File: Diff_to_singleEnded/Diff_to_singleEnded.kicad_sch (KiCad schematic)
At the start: 45 parts, among them IC1 ULN2003LVDR, J1 1725672, J2 1725672, J3 1725672, J4 1725672, J5 1725672, J6 1725672, J7 1725672, K3 EE2-5NU, U1 OPA1692xD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

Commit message: removed Relay and power supples related items from board and add seperate ground plains for signal and power
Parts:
- removed C11: 100n, Capacitor_SMD:C_0805_2012Metric_Pad1.18x1.45mm_HandSolder, symbol Device:C
- removed IC1: ULN2003LVDR, samsys:SOIC127P780X200-16N, symbol SamaSys:ULN2003LVDR
- removed J2, J6, J7: 1725672, 1725672, symbol NewSamsys:1725672
- removed K3: EE2-5NU, EE2-5NU, symbol NewSamsys:EE2-5NU
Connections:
- net right in is gone; now on net Rout: C2.2, R10.2, U3.7
- net right out is gone; now on net Lout: J3.1
- net GND: no longer C13.1, C14.1, C15.1, J3.2, J3.3, J4.2, J4.3, J5.2, J5.3, R5.2, R6.1, R8.1
- net Left Out renamed Rout
- net Left in renamed Lout
- new net GND 2: C13.1, C14.1, C15.1, J3.2, J3.3, J4.2, J4.3, J5.2, J5.3, R5.2, R6.1, R8.1
- no-connect marks 14 -> 0
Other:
- moved on the sheet: C1, C10, C12, C13, C14, C15, C2, C3, C4, C5, C6, C7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

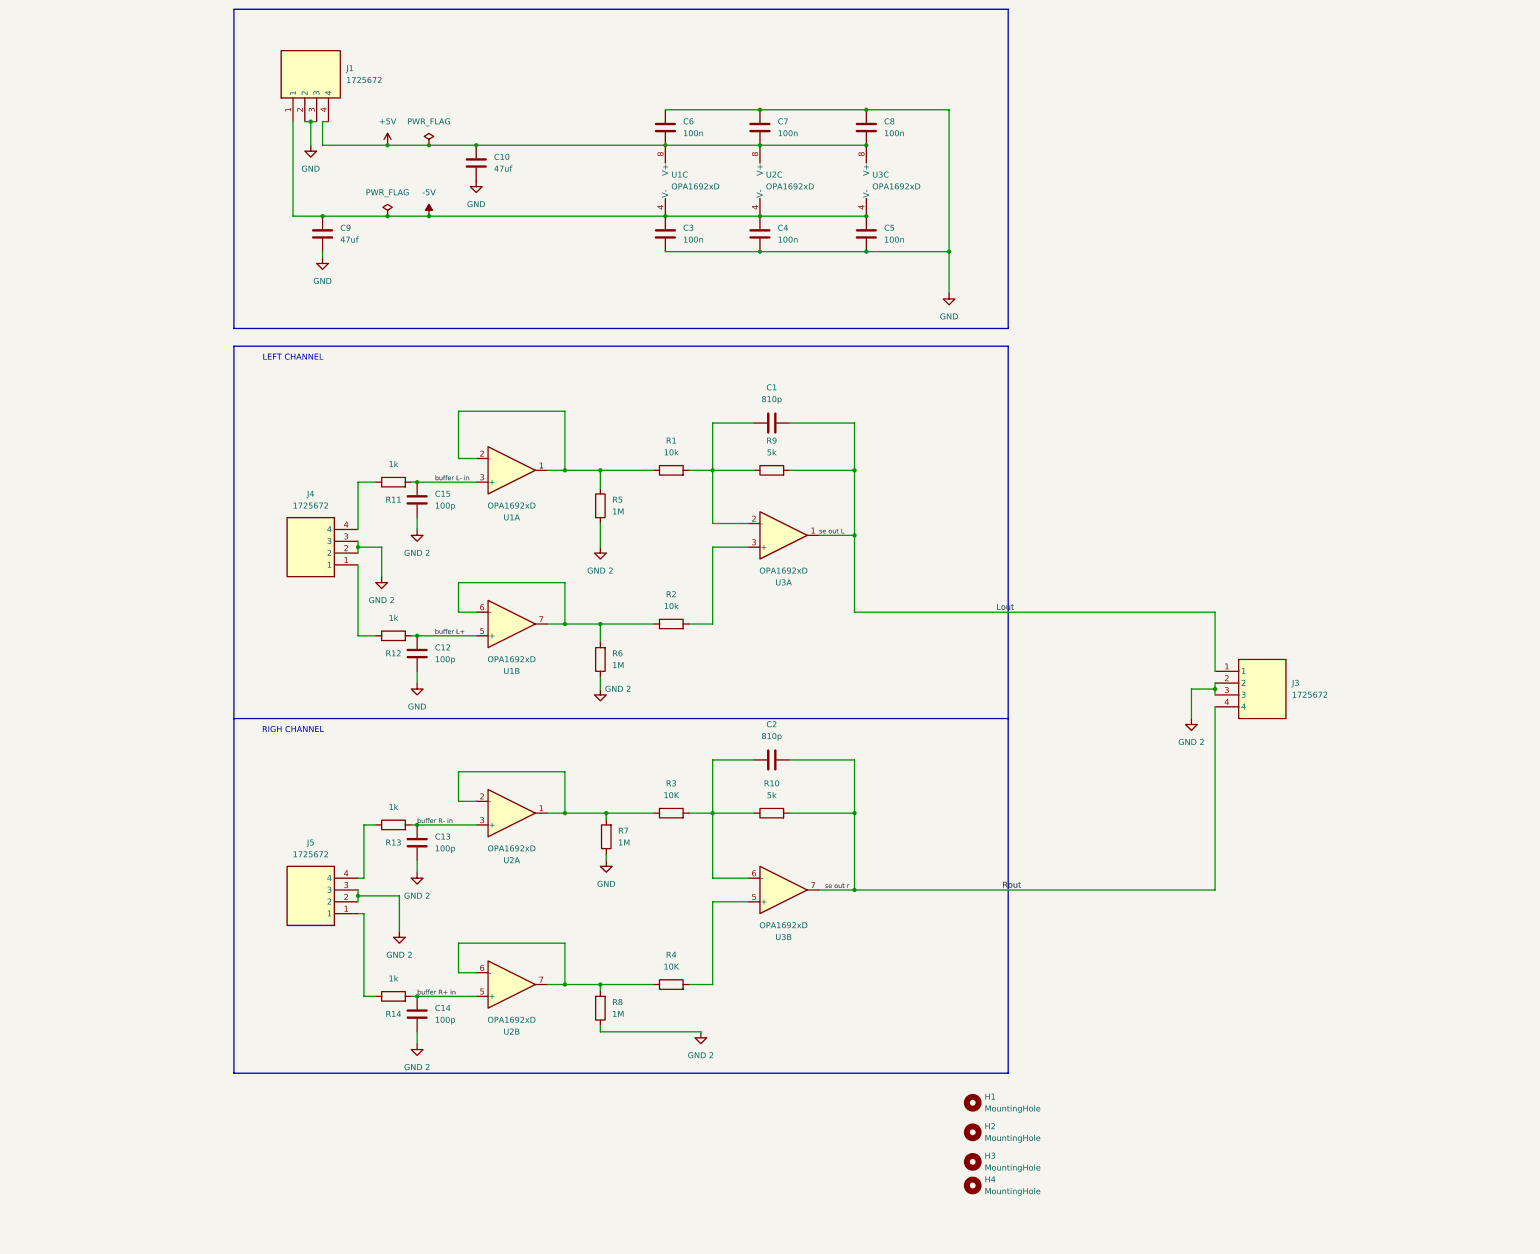
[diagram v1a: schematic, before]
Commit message: added new rpi power board
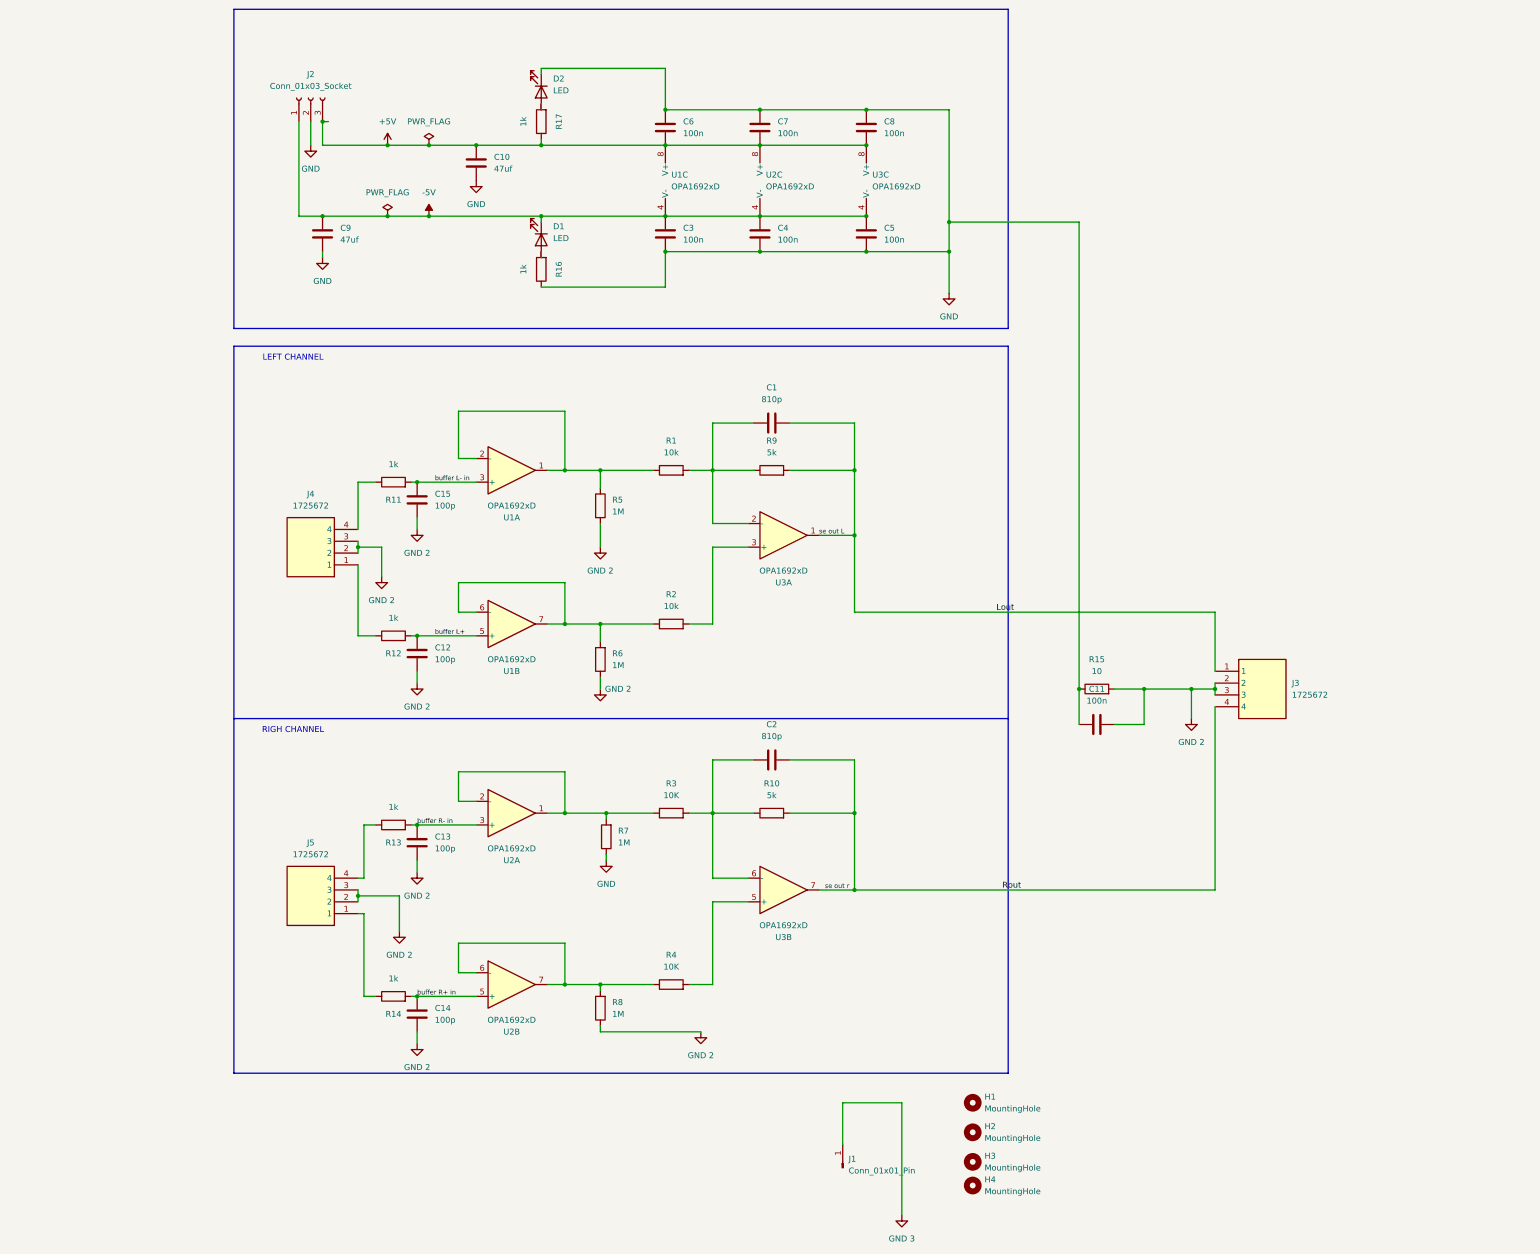
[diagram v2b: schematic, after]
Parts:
- removed J1: 1725672, 1725672, symbol NewSamsys:1725672
- added C11: 100n, Capacitor_SMD:C_0805_2012Metric_Pad1.18x1.45mm_HandSolder, symbol Device:C
- added D1, D2: LED, samsys:LEDC2012X40N, symbol Device:LED
- added J1: Conn_01x01_Pin, Connector_PinHeader_1.00mm:PinHeader_1x01_P1.00mm_Vertical, symbol Connector:Conn_01x01_Pin
- added J2: Conn_01x03_Socket, Connector_Phoenix_MC:PhoenixContact_MCV_1,5_3-G-3.81_1x03_P3.81mm_Vertical, symbol Connector:Conn_01x03_Socket
- added R15: 10, Resistor_SMD:R_0603_1608Metric, symbol Device:R
- added R16, R17: 1k, Resistor_SMD:R_0805_2012Metric, symbol Device:R
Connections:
- net +5V: now also J2.3 (Pin_3), R17.1
- net -5V: now also D1.1 (K), J2.1 (Pin_1)
- net GND: now also C11.1, D2.1 (K), J2.2 (Pin_2), R15.1, R16.1; no longer C12.1
- net GND 2: now also C12.1, C11.2, R15.2
- new net: D1.2 (A), R16.2
- new net: D2.2 (A), R17.2
- new net GND 3: J1.1 (Pin_1)

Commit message: add updates to se to diff
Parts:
- removed J3, J4, J5: 1725672, 1725672, symbol NewSamsys:1725672
- added J6, J7, J8: 1725669, 1725669, symbol NewSamsys:1725669
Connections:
- net GND 2: now also J6.2, J7.2, J8.2
- net Lout: now also J8.3
- net Rout: now also J8.1
- net at R12.1: now also J6.3
- net at R11.1: now also J6.1
- net at R14.1: now also J7.3
- net at R13.1: now also J7.1

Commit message: updated final four boards for streamer
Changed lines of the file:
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@@
 		(on_board yes)
 		(dnp no)
-		(fields_autoplaced yes)
 		(property "Reference" "C11"
-			(at 267.97 160.02 90)
+			(at 267.97 171.45 90)
 			(effects
 				(font
@@
 		)
 		(property "Value" "100n"
-			(at 267.97 162.56 90)
+			(at 267.97 173.99 90)
 			(effects
 				(font
